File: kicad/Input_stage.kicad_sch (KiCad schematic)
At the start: 57 parts

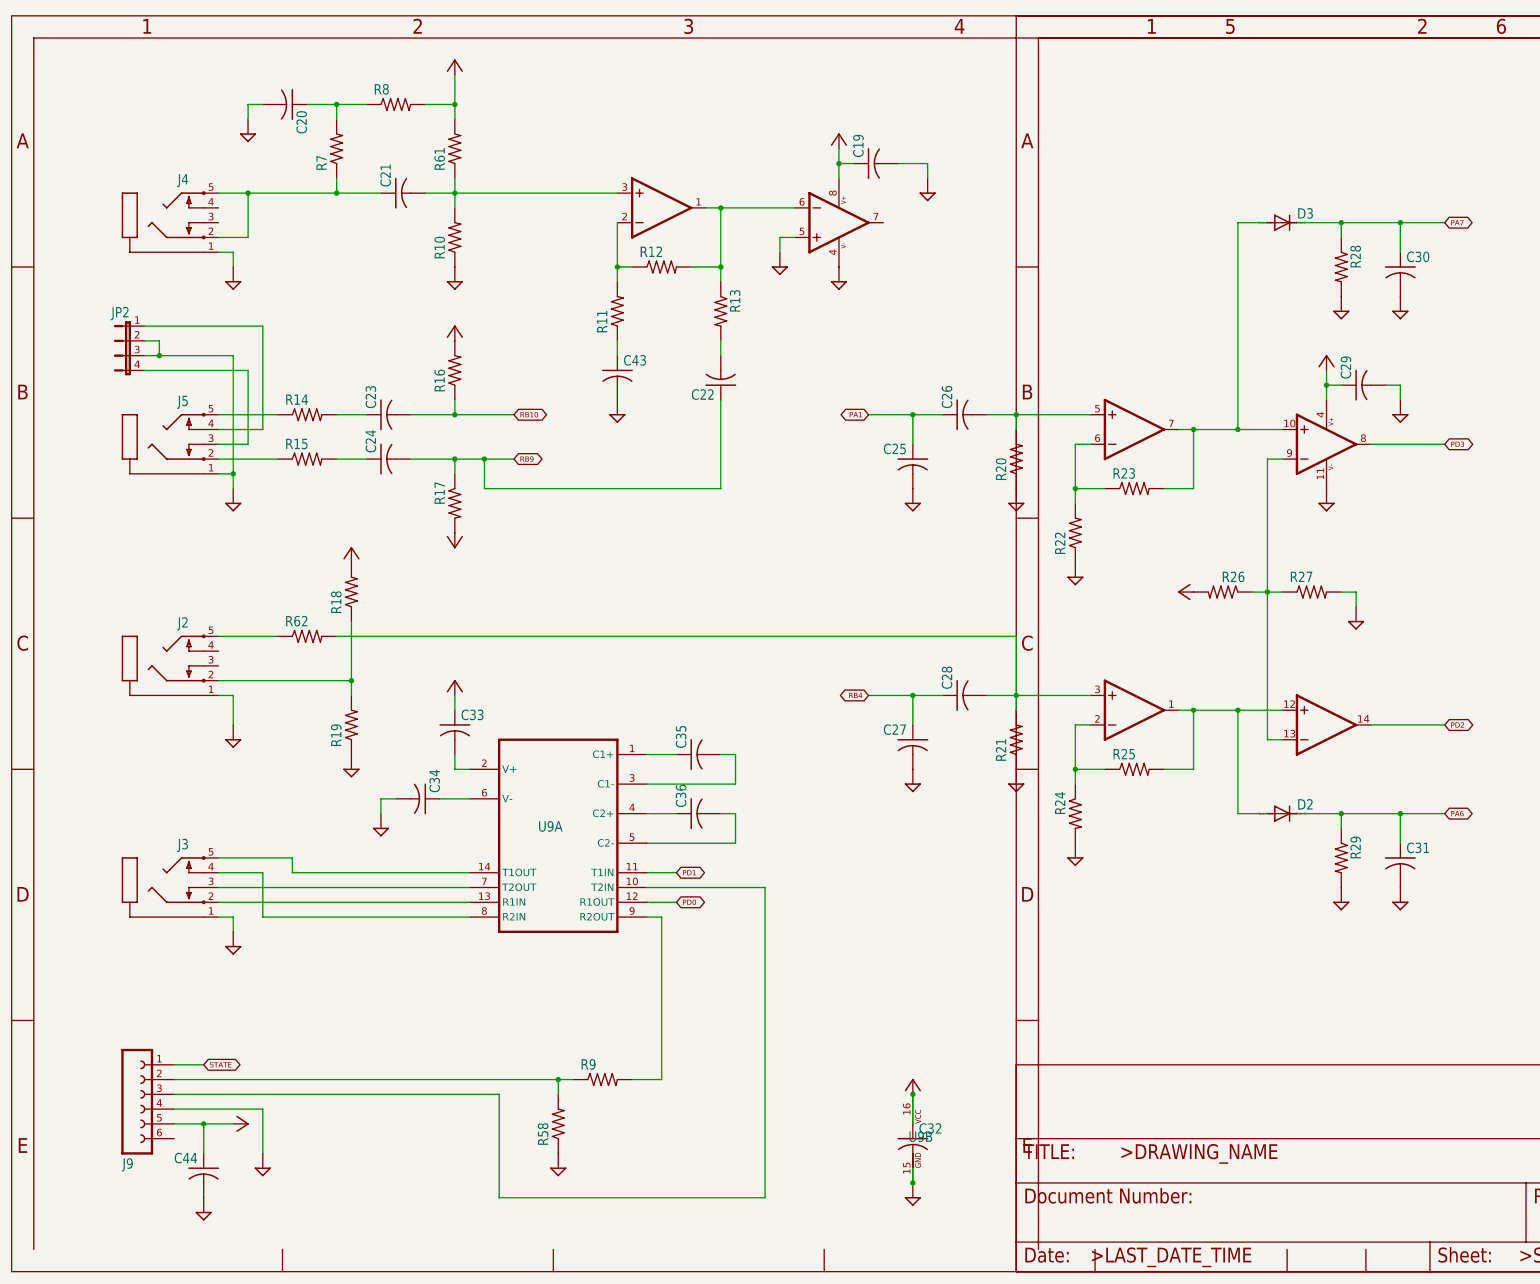
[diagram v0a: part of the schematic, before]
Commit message: Conversion of display print to KiCad components; still attached to main board
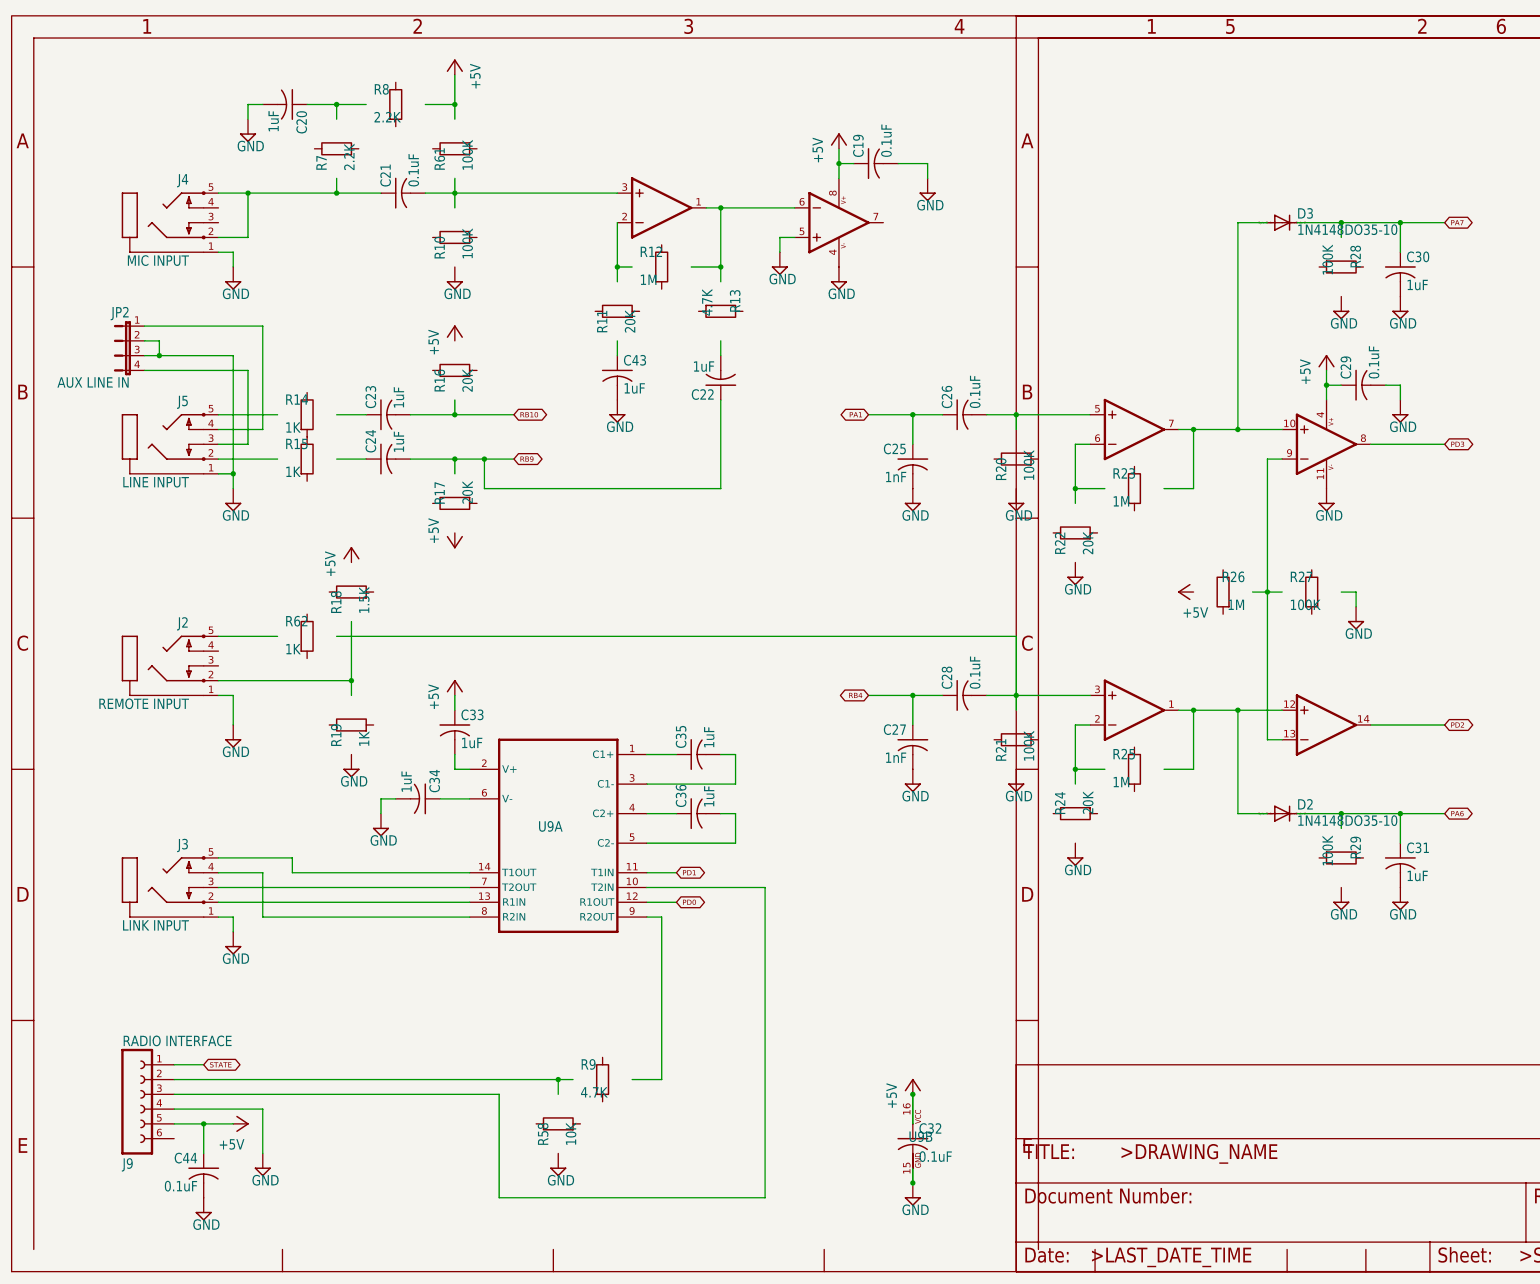
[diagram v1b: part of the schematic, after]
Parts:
- C19, C21, C26, C28, C29, C32, C44: value (none) -> 0.1uF; footprint (none) -> mk312:C025-024X044
- C20, C22, C23, C24, C30, C31, C33, C34, C35, C36, C43: value (none) -> 1uF; footprint (none) -> mk312:C025-024X044
- C25, C27: value (none) -> 1nF; footprint (none) -> mk312:C025-024X044
- D2, D3: value (none) -> 1N4148DO35-10; footprint (none) -> mk312:DO35-10
- J2: value (none) -> REMOTE INPUT; footprint (none) -> mk312:STX3100
- J3: value (none) -> LINK INPUT; footprint (none) -> mk312:STX3100
- J4: value (none) -> MIC INPUT; footprint (none) -> mk312:STX3100
- J5: value (none) -> LINE INPUT; footprint (none) -> mk312:STX3100
- J9: value (none) -> RADIO INTERFACE; footprint (none) -> mk312:FE06
- JP2: value (none) -> AUX LINE IN; footprint (none) -> mk312:JP4
- R10, R20, R21, R27, R28, R29, R61: value (none) -> 100K; footprint (none) -> mk312:0207_10; symbol mk312-eagle-import:R-US_0207/10 -> Device:R
- R11, R16, R17, R22, R24: value (none) -> 20K; footprint (none) -> mk312:0207_10; symbol mk312-eagle-import:R-US_0207/10 -> Device:R
- R12, R23, R25, R26: value (none) -> 1M; footprint (none) -> mk312:0207_10; symbol mk312-eagle-import:R-US_0207/10 -> Device:R
- R13, R9: value (none) -> 4.7K; footprint (none) -> mk312:0207_10; symbol mk312-eagle-import:R-US_0207/10 -> Device:R
- R14, R15, R19, R62: value (none) -> 1K; footprint (none) -> mk312:0207_10; symbol mk312-eagle-import:R-US_0207/10 -> Device:R
- R18: value (none) -> 1.5K; footprint (none) -> mk312:0207_10; symbol mk312-eagle-import:R-US_0207/10 -> Device:R
- R58: value (none) -> 10K; footprint (none) -> mk312:0207_10; symbol mk312-eagle-import:R-US_0207/10 -> Device:R
- R7, R8: value (none) -> 2.2K; footprint (none) -> mk312:0207_10; symbol mk312-eagle-import:R-US_0207/10 -> Device:R
- U2: value (none) -> LM324N; footprint (none) -> mk312:DIL14
- U4: value (none) -> LM358N; footprint (none) -> mk312:DIL08
- U9: value (none) -> MAX232; footprint (none) -> mk312:DIL16
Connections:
- net +5V: no longer R16.2, R17.2, R18.2, R26.2, R61.2, R8.2
- net GND: no longer R10.1, R19.1, R20.1, R21.1, R22.1, R24.2, R27.2, R28.2, R29.2, R58.1
- net PA6: no longer R29.1
- net PA7: no longer R28.1
- net RB10: no longer R16.1
- net RB9: no longer R17.1
- net at C21.1, J4.2, J4.5: no longer R7.1
- net at C21.2, U4.3 (+IN): no longer R10.2, R61.1
- net at U2.13 (-IN), U2.9 (-IN): no longer R26.1, R27.1
- net at D2.A, U2.1 (OUT), U2.12 (+IN): no longer R25.2
- net at D3.A, U2.10 (+IN), U2.7 (OUT): no longer R23.2
- net at R14.1: no longer J5.5
- net at R14.2: now also R15.1; no longer C23.1
- net at C28.2, U2.3 (+IN): no longer R21.2, R62.2
- net at C24.1: no longer R15.2
- net at R11.1: no longer C43.1
- net at U4.1 (OUT), U4.6 (-IN): no longer R12.2, R13.1
- net at R13.2: no longer C22.2
- net at C26.2, U2.5 (+IN): no longer R20.2
- net at R62.1: no longer J2.5
- net at J5.2: no longer R15.1
- net at R9.2: no longer U9.9 (R2OUT)
- now unconnected: C20.1, J2.2, J9.2, R11.2, R12.1, R18.1, R19.2, R22.2, R23.1, R24.1, R25.1, R58.2, R7.2, R8.1, R9.1, U2.2 (-IN), U2.6 (-IN), U4.2 (-IN)
